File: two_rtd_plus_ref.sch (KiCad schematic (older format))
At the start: 18 parts

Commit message: completed schematic
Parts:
- C10, C11, C12, C13, C14, C15: renamed from C?; value C -> 5nF
- C7, C8, C9: renamed from C?; value C -> 50nF
- R10, R11, R12, R7, R8, R9: renamed from R?; value R -> 5k
- R6: renamed from R?; value R -> 2k
- gave numbers to parts that had none: 2

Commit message: finished schematic, assigned footprints, generated netlist
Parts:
- C10, C11, C12, C13, C14, C15, C7, C8, C9: footprint (none) -> Capacitor_SMD:C_0805_2012Metric_Pad1.15x1.40mm_HandSolder
- J3, J4: footprint (none) -> temp4x4:screw_term_4x
- R10, R11, R12, R6, R7, R8, R9: footprint (none) -> Resistor_SMD:R_0805_2012Metric_Pad1.15x1.40mm_HandSolder
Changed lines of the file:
@@
 AR Path="/5EC374D6/5EC48F50" Ref="J3"  Part="1"
 AR Path="/5ED0B429/5EC48F50" Ref="J5"  Part="1"
-F 0 "J5" H 3968 2917 50  0000 C CNN
+F 0 "J3" H 3968 2917 50  0000 C CNN
 F 1 "4-wire RTD" H 3968 2826 50  0000 C CNN
-F 2 "" H 4050 2600 50  0001 C CNN
+F 2 "temp4x4:screw_term_4x" H 4050 2600 50  0001 C CNN
 F 3 "~" H 4050 2600 50  0001 C CNN
 	1    4050 2600
@@
 AR Path="/5EC374D6/5EC48F56" Ref="C11"  Part="1"
 AR Path="/5ED0B429/5EC48F56" Ref="C20"  Part="1"
-F 0 "C20" H 5565 2846 50  0000 L CNN
+F 0 "C11" H 5565 2846 50  0000 L CNN
 F 1 "5nF" H 5565 2755 50  0000 L CNN
-F 2 "" H 5488 2650 50  0001 C CNN
+F 2 "Capacitor_SMD:C_0805_2012Metric_Pad1.15x1.40mm_HandSolder" H 5488 2650 50  0001 C CNN
 F 3 "~" H 5450 2800 50  0001 C CNN
 	1    5450 2800
@@
 AR Path="/5EC374D6/5EC48F5C" Ref="C7"  Part="1"
 AR Path="/5ED0B429/5EC48F5C" Ref="C16"  Part="1"
-F 0 "C16" H 5215 2696 50  0000 L CNN
+F 0 "C7" H 5215 2696 50  0000 L CNN
 F 1 "50nF" H 5215 2605 50  0000 L CNN
-F 2 "" H 5138 2500 50  0001 C CNN
+F 2 "Capacitor_SMD:C_0805_2012Metric_Pad1.15x1.40mm_HandSolder" H 5138 2500 50  0001 C CNN
 F 3 "~" H 5100 2650 50  0001 C CNN
 	1    5100 2650
@@
 AR Path="/5EC374D6/5EC48F62" Ref="C10"  Part="1"
 AR Path="/5ED0B429/5EC48F62" Ref="C19"  Part="1"
-F 0 "C19" H 5565 2546 50  0000 L CNN
+F 0 "C10" H 5565 2546 50  0000 L CNN
 F 1 "5nF" H 5565 2455 50  0000 L CNN
-F 2 "" H 5488 2350 50  0001 C CNN
+F 2 "Capacitor_SMD:C_0805_2012Metric_Pad1.15x1.40mm_HandSolder" H 5488 2350 50  0001 C CNN
 F 3 "~" H 5450 2500 50  0001 C CNN
 	1    5450 2500
@@
 AR Path="/5EC374D6/5EC48F68" Ref="#PWR014"  Part="1"
 AR Path="/5ED0B429/5EC48F68" Ref="#PWR017"  Part="1"
-F 0 "#PWR017" H 5650 2400 50  0001 C CNN
+F 0 "#PWR014" H 5650 2400 50  0001 C CNN
 F 1 "Earth" H 5650 2500 50  0001 C CNN
 F 2 "" H 5650 2650 50  0001 C CNN
@@
 AR Path="/5EC374D6/5EC48F74" Ref="R9"  Part="1"
 AR Path="/5ED0B429/5EC48F74" Ref="R16"  Part="1"
-F 0 "R16" V 5057 2350 50  0000 C CNN
+F 0 "R9" V 5057 2350 50  0000 C CNN
 F 1 "5k" V 4966 2350 50  0000 C CNN
-F 2 "" V 4780 2350 50  0001 C CNN
+F 2 "Resistor_SMD:R_0805_2012Metric_Pad1.15x1.40mm_HandSolder" V 4780 2350 50  0001 C CNN
 F 3 "~" H 4850 2350 50  0001 C CNN
 	1    4850 2350
@@
 AR Path="/5EC374D6/5EC48F7B" Ref="R10"  Part="1"
 AR Path="/5ED0B429/5EC48F7B" Ref="R17"  Part="1"
-F 0 "R17" V 5057 2950 50  0000 C CNN
+F 0 "R10" V 5057 2950 50  0000 C CNN
 F 1 "5k" V 4966 2950 50  0000 C CNN
-F 2 "" V 4780 2950 50  0001 C CNN
+F 2 "Resistor_SMD:R_0805_2012Metric_Pad1.15x1.40mm_HandSolder" V 4780 2950 50  0001 C CNN
 F 3 "~" H 4850 2950 50  0001 C CNN
 	1    4850 2950
@@
 AR Path="/5EC374D6/5EC48F91" Ref="J4"  Part="1"
 AR Path="/5ED0B429/5EC48F91" Ref="J6"  Part="1"
-F 0 "J6" H 3968 3967 50  0000 C CNN
+F 0 "J4" H 3968 3967 50  0000 C CNN
 F 1 "4-wire RTD" H 3968 3876 50  0000 C CNN
-F 2 "" H 4050 3650 50  0001 C CNN
+F 2 "temp4x4:screw_term_4x" H 4050 3650 50  0001 C CNN
 F 3 "~" H 4050 3650 50  0001 C CNN
 	1    4050 3650
@@
 AR Path="/5EC374D6/5EC48F97" Ref="C13"  Part="1"
 AR Path="/5ED0B429/5EC48F97" Ref="C22"  Part="1"
-F 0 "C22" H 5565 3896 50  0000 L CNN
+F 0 "C13" H 5565 3896 50  0000 L CNN
 F 1 "5nF" H 5565 3805 50  0000 L CNN
-F 2 "" H 5488 3700 50  0001 C CNN
+F 2 "Capacitor_SMD:C_0805_2012Metric_Pad1.15x1.40mm_HandSolder" H 5488 3700 50  0001 C CNN
 F 3 "~" H 5450 3850 50  0001 C CNN
 	1    5450 3850
@@
 AR Path="/5EC374D6/5EC48F9D" Ref="C8"  Part="1"
 AR Path="/5ED0B429/5EC48F9D" Ref="C17"  Part="1"
-F 0 "C17" H 5215 3746 50  0000 L CNN
+F 0 "C8" H 5215 3746 50  0000 L CNN
 F 1 "50nF" H 5215 3655 50  0000 L CNN
-F 2 "" H 5138 3550 50  0001 C CNN
+F 2 "Capacitor_SMD:C_0805_2012Metric_Pad1.15x1.40mm_HandSolder" H 5138 3550 50  0001 C CNN
 F 3 "~" H 5100 3700 50  0001 C CNN
 	1    5100 3700
@@
 AR Path="/5EC374D6/5EC48FA3" Ref="C12"  Part="1"
 AR Path="/5ED0B429/5EC48FA3" Ref="C21"  Part="1"
-F 0 "C21" H 5565 3596 50  0000 L CNN
+F 0 "C12" H 5565 3596 50  0000 L CNN
 F 1 "5nF" H 5565 3505 50  0000 L CNN
-F 2 "" H 5488 3400 50  0001 C CNN
+F 2 "Capacitor_SMD:C_0805_2012Metric_Pad1.15x1.40mm_HandSolder" H 5488 3400 50  0001 C CNN
 F 3 "~" H 5450 3550 50  0001 C CNN
 	1    5450 3550
@@
 AR Path="/5EC374D6/5EC48FA9" Ref="#PWR015"  Part="1"
 AR Path="/5ED0B429/5EC48FA9" Ref="#PWR018"  Part="1"
-F 0 "#PWR018" H 5650 3450 50  0001 C CNN
+F 0 "#PWR015" H 5650 3450 50  0001 C CNN
 F 1 "Earth" H 5650 3550 50  0001 C CNN
 F 2 "" H 5650 3700 50  0001 C CNN
@@
 AR Path="/5EC374D6/5EC48FB5" Ref="R11"  Part="1"
 AR Path="/5ED0B429/5EC48FB5" Ref="R18"  Part="1"
-F 0 "R18" V 5057 3400 50  0000 C CNN
+F 0 "R11" V 5057 3400 50  0000 C CNN
 F 1 "5k" V 4966 3400 50  0000 C CNN
-F 2 "" V 4780 3400 50  0001 C CNN
+F 2 "Resistor_SMD:R_0805_2012Metric_Pad1.15x1.40mm_HandSolder" V 4780 3400 50  0001 C CNN
 F 3 "~" H 4850 3400 50  0001 C CNN
 	1    4850 3400
@@
 AR Path="/5EC374D6/5EC48FBC" Ref="R12"  Part="1"
 AR Path="/5ED0B429/5EC48FBC" Ref="R19"  Part="1"
-F 0 "R19" V 5057 4000 50  0000 C CNN
+F 0 "R12" V 5057 4000 50  0000 C CNN
 F 1 "5k" V 4966 4000 50  0000 C CNN
-F 2 "" V 4780 4000 50  0001 C CNN
+F 2 "Resistor_SMD:R_0805_2012Metric_Pad1.15x1.40mm_HandSolder" V 4780 4000 50  0001 C CNN
 F 3 "~" H 4850 4000 50  0001 C CNN
 	1    4850 4000
@@
 AR Path="/5EC374D6/5EC48FD1" Ref="C15"  Part="1"
 AR Path="/5ED0B429/5EC48FD1" Ref="C24"  Part="1"
-F 0 "C24" H 5565 4946 50  0000 L CNN
+F 0 "C15" H 5565 4946 50  0000 L CNN
 F 1 "5nF" H 5565 4855 50  0000 L CNN
-F 2 "" H 5488 4750 50  0001 C CNN
+F 2 "Capacitor_SMD:C_0805_2012Metric_Pad1.15x1.40mm_HandSolder" H 5488 4750 50  0001 C CNN
 F 3 "~" H 5450 4900 50  0001 C CNN
 	1    5450 4900
@@
 AR Path="/5EC374D6/5EC48FD7" Ref="C9"  Part="1"
 AR Path="/5ED0B429/5EC48FD7" Ref="C18"  Part="1"
-F 0 "C18" H 5215 4796 50  0000 L CNN
+F 0 "C9" H 5215 4796 50  0000 L CNN
 F 1 "50nF" H 5215 4705 50  0000 L CNN
-F 2 "" H 5138 4600 50  0001 C CNN
+F 2 "Capacitor_SMD:C_0805_2012Metric_Pad1.15x1.40mm_HandSolder" H 5138 4600 50  0001 C CNN
 F 3 "~" H 5100 4750 50  0001 C CNN
 	1    5100 4750
@@
 AR Path="/5EC374D6/5EC48FDD" Ref="C14"  Part="1"
 AR Path="/5ED0B429/5EC48FDD" Ref="C23"  Part="1"
-F 0 "C23" H 5565 4646 50  0000 L CNN
+F 0 "C14" H 5565 4646 50  0000 L CNN
 F 1 "5nF" H 5565 4555 50  0000 L CNN
-F 2 "" H 5488 4450 50  0001 C CNN
+F 2 "Capacitor_SMD:C_0805_2012Metric_Pad1.15x1.40mm_HandSolder" H 5488 4450 50  0001 C CNN
 F 3 "~" H 5450 4600 50  0001 C CNN
 	1    5450 4600
@@
 AR Path="/5EC374D6/5EC48FE3" Ref="#PWR016"  Part="1"
 AR Path="/5ED0B429/5EC48FE3" Ref="#PWR019"  Part="1"
-F 0 "#PWR019" H 5650 4500 50  0001 C CNN
+F 0 "#PWR016" H 5650 4500 50  0001 C CNN
 F 1 "Earth" H 5650 4600 50  0001 C CNN
 F 2 "" H 5650 4750 50  0001 C CNN
@@
 AR Path="/5EC374D6/5EC48FEF" Ref="R7"  Part="1"
 AR Path="/5ED0B429/5EC48FEF" Ref="R14"  Part="1"
-F 0 "R14" V 5007 4450 50  0000 C CNN
+F 0 "R7" V 5007 4450 50  0000 C CNN
 F 1 "5k" V 4916 4450 50  0000 C CNN
-F 2 "" V 4730 4450 50  0001 C CNN
+F 2 "Resistor_SMD:R_0805_2012Metric_Pad1.15x1.40mm_HandSolder" V 4730 4450 50  0001 C CNN
 F 3 "~" H 4800 4450 50  0001 C CNN
 	1    4800 4450
@@
 AR Path="/5EC374D6/5EC48FF6" Ref="R8"  Part="1"
 AR Path="/5ED0B429/5EC48FF6" Ref="R15"  Part="1"
-F 0 "R15" V 5007 5050 50  0000 C CNN
+F 0 "R8" V 5007 5050 50  0000 C CNN
 F 1 "5k" V 4916 5050 50  0000 C CNN
-F 2 "" V 4730 5050 50  0001 C CNN
+F 2 "Resistor_SMD:R_0805_2012Metric_Pad1.15x1.40mm_HandSolder" V 4730 5050 50  0001 C CNN
 F 3 "~" H 4800 5050 50  0001 C CNN
 	1    4800 5050
@@
 AR Path="/5EC374D6/5EC49006" Ref="R6"  Part="1"
 AR Path="/5ED0B429/5EC49006" Ref="R13"  Part="1"
-F 0 "R13" H 4520 4796 50  0000 L CNN
+F 0 "R6" H 4520 4796 50  0000 L CNN
 F 1 "2k" H 4520 4705 50  0000 L CNN
-F 2 "" V 4380 4750 50  0001 C CNN
+F 2 "Resistor_SMD:R_0805_2012Metric_Pad1.15x1.40mm_HandSolder" V 4380 4750 50  0001 C CNN
 F 3 "~" H 4450 4750 50  0001 C CNN
 	1    4450 4750

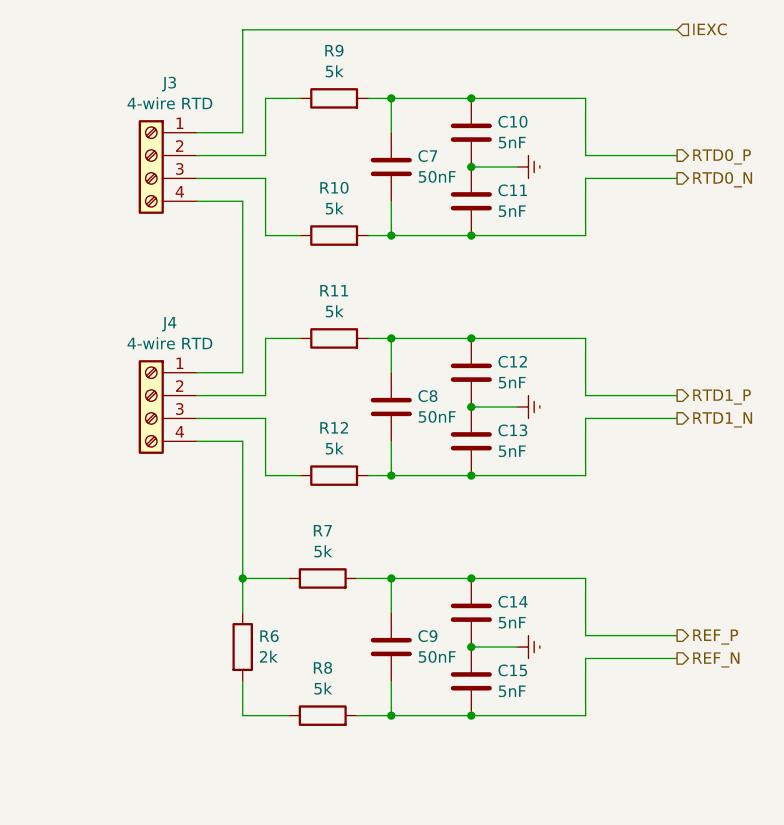
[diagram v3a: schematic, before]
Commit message: added jumper to bypass 2nd RTD
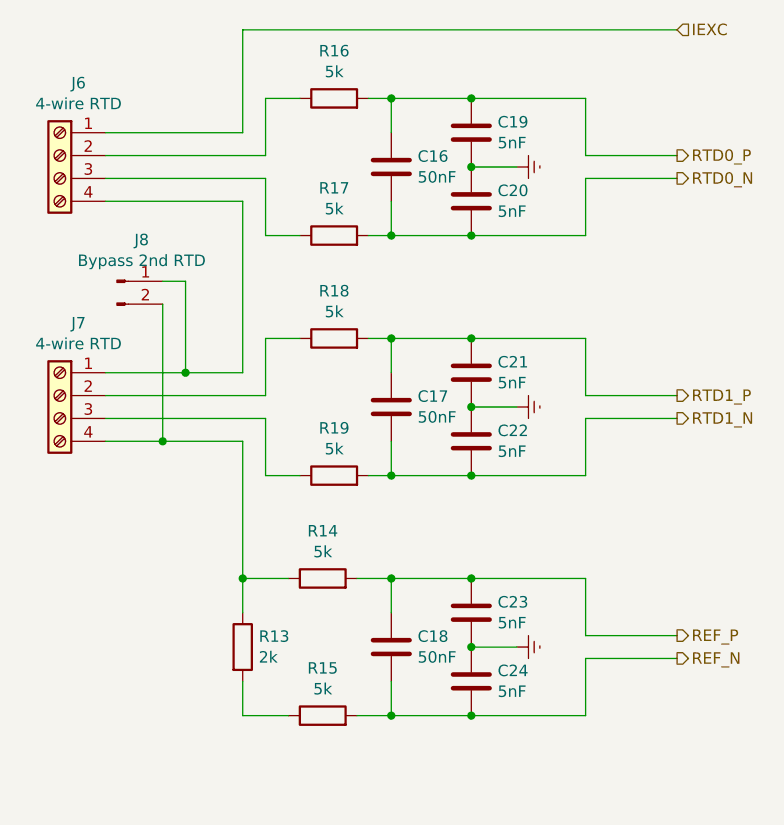
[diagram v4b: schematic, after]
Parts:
- added J5: Bypass 2nd RTD, symbol Connector:Conn_01x02_Male
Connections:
- net at J3.4 (Pin_4), J4.1 (Pin_1): now also J5.1 (Pin_1)
- net at J4.4 (Pin_4), R6.1, R7.1: now also J5.2 (Pin_2)
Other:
- moved on the sheet: J6, J7
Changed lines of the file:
@@
 L Connector:Screw_Terminal_01x04 J3
 U 1 1 5EC48F50
-P 4050 2600
+P 3650 2600
 AR Path="/5EC374D6/5EC48F50" Ref="J3"  Part="1"
-AR Path="/5ED0B429/5EC48F50" Ref="J5"  Part="1"
-F 0 "J3" H 3968 2917 50  0000 C CNN
-F 1 "4-wire RTD" H 3968 2826 50  0000 C CNN
-F 2 "temp4x4:screw_term_4x" H 4050 2600 50  0001 C CNN
-F 3 "~" H 4050 2600 50  0001 C CNN
-	1    4050 2600
+AR Path="/5ED0B429/5EC48F50" Ref="J6"  Part="1"
+F 0 "J6" H 3568 2917 50  0000 C CNN
+F 1 "4-wire RTD" H 3568 2826 50  0000 C CNN
+F 2 "temp4x4:screw_term_4x" H 3650 2600 50  0001 C CNN
+F 3 "~" H 3650 2600 50  0001 C CNN
+	1    3650 2600
 	-1   0    0    -1
 $EndComp
@@
 AR Path="/5EC374D6/5EC48F56" Ref="C11"  Part="1"
 AR Path="/5ED0B429/5EC48F56" Ref="C20"  Part="1"
-F 0 "C11" H 5565 2846 50  0000 L CNN
+F 0 "C20" H 5565 2846 50  0000 L CNN
 F 1 "5nF" H 5565 2755 50  0000 L CNN
 F 2 "Capacitor_SMD:C_0805_2012Metric_Pad1.15x1.40mm_HandSolder" H 5488 2650 50  0001 C CNN
@@
 AR Path="/5EC374D6/5EC48F5C" Ref="C7"  Part="1"
 AR Path="/5ED0B429/5EC48F5C" Ref="C16"  Part="1"
-F 0 "C7" H 5215 2696 50  0000 L CNN
+F 0 "C16" H 5215 2696 50  0000 L CNN
 F 1 "50nF" H 5215 2605 50  0000 L CNN
 F 2 "Capacitor_SMD:C_0805_2012Metric_Pad1.15x1.40mm_HandSolder" H 5138 2500 50  0001 C CNN
@@
 AR Path="/5EC374D6/5EC48F62" Ref="C10"  Part="1"
 AR Path="/5ED0B429/5EC48F62" Ref="C19"  Part="1"
-F 0 "C10" H 5565 2546 50  0000 L CNN
+F 0 "C19" H 5565 2546 50  0000 L CNN
 F 1 "5nF" H 5565 2455 50  0000 L CNN
 F 2 "Capacitor_SMD:C_0805_2012Metric_Pad1.15x1.40mm_HandSolder" H 5488 2350 50  0001 C CNN
@@
 AR Path="/5EC374D6/5EC48F68" Ref="#PWR014"  Part="1"
 AR Path="/5ED0B429/5EC48F68" Ref="#PWR017"  Part="1"
-F 0 "#PWR014" H 5650 2400 50  0001 C CNN
+F 0 "#PWR017" H 5650 2400 50  0001 C CNN
 F 1 "Earth" H 5650 2500 50  0001 C CNN
 F 2 "" H 5650 2650 50  0001 C CNN
@@
 AR Path="/5EC374D6/5EC48F74" Ref="R9"  Part="1"
 AR Path="/5ED0B429/5EC48F74" Ref="R16"  Part="1"
-F 0 "R9" V 5057 2350 50  0000 C CNN
+F 0 "R16" V 5057 2350 50  0000 C CNN
 F 1 "5k" V 4966 2350 50  0000 C CNN
 F 2 "Resistor_SMD:R_0805_2012Metric_Pad1.15x1.40mm_HandSolder" V 4780 2350 50  0001 C CNN
@@
 AR Path="/5EC374D6/5EC48F7B" Ref="R10"  Part="1"
 AR Path="/5ED0B429/5EC48F7B" Ref="R17"  Part="1"
-F 0 "R10" V 5057 2950 50  0000 C CNN
+F 0 "R17" V 5057 2950 50  0000 C CNN
 F 1 "5k" V 4966 2950 50  0000 C CNN
 F 2 "Resistor_SMD:R_0805_2012Metric_Pad1.15x1.40mm_HandSolder" V 4780 2950 50  0001 C CNN
@@
 Connection ~ 5100 2950
 Wire Wire Line
-	4250 2600 4550 2600
-Wire Wire Line
 	4550 2600 4550 2350
 Wire Wire Line
 	4550 2350 4700 2350
-Wire Wire Line
-	4250 2700 4550 2700
 Wire Wire Line
 	4550 2700 4550 2950
@@
 L Connector:Screw_Terminal_01x04 J4
 U 1 1 5EC48F91
-P 4050 3650
+P 3650 3650
 AR Path="/5EC374D6/5EC48F91" Ref="J4"  Part="1"
-AR Path="/5ED0B429/5EC48F91" Ref="J6"  Part="1"
-F 0 "J4" H 3968 3967 50  0000 C CNN
-F 1 "4-wire RTD" H 3968 3876 50  0000 C CNN
-F 2 "temp4x4:screw_term_4x" H 4050 3650 50  0001 C CNN
-F 3 "~" H 4050 3650 50  0001 C CNN
-	1    4050 3650
+AR Path="/5ED0B429/5EC48F91" Ref="J7"  Part="1"
+F 0 "J7" H 3568 3967 50  0000 C CNN
+F 1 "4-wire RTD" H 3568 3876 50  0000 C CNN
+F 2 "temp4x4:screw_term_4x" H 3650 3650 50  0001 C CNN
+F 3 "~" H 3650 3650 50  0001 C CNN
+	1    3650 3650
 	-1   0    0    -1
 $EndComp
@@
 AR Path="/5EC374D6/5EC48F97" Ref="C13"  Part="1"
 AR Path="/5ED0B429/5EC48F97" Ref="C22"  Part="1"
-F 0 "C13" H 5565 3896 50  0000 L CNN
+F 0 "C22" H 5565 3896 50  0000 L CNN
 F 1 "5nF" H 5565 3805 50  0000 L CNN
 F 2 "Capacitor_SMD:C_0805_2012Metric_Pad1.15x1.40mm_HandSolder" H 5488 3700 50  0001 C CNN
@@
 AR Path="/5EC374D6/5EC48F9D" Ref="C8"  Part="1"
 AR Path="/5ED0B429/5EC48F9D" Ref="C17"  Part="1"
-F 0 "C8" H 5215 3746 50  0000 L CNN
+F 0 "C17" H 5215 3746 50  0000 L CNN
 F 1 "50nF" H 5215 3655 50  0000 L CNN
 F 2 "Capacitor_SMD:C_0805_2012Metric_Pad1.15x1.40mm_HandSolder" H 5138 3550 50  0001 C CNN
@@
 AR Path="/5EC374D6/5EC48FA3" Ref="C12"  Part="1"
 AR Path="/5ED0B429/5EC48FA3" Ref="C21"  Part="1"
-F 0 "C12" H 5565 3596 50  0000 L CNN
+F 0 "C21" H 5565 3596 50  0000 L CNN
 F 1 "5nF" H 5565 3505 50  0000 L CNN
 F 2 "Capacitor_SMD:C_0805_2012Metric_Pad1.15x1.40mm_HandSolder" H 5488 3400 50  0001 C CNN
@@
 AR Path="/5EC374D6/5EC48FA9" Ref="#PWR015"  Part="1"
 AR Path="/5ED0B429/5EC48FA9" Ref="#PWR018"  Part="1"
-F 0 "#PWR015" H 5650 3450 50  0001 C CNN
+F 0 "#PWR018" H 5650 3450 50  0001 C CNN
 F 1 "Earth" H 5650 3550 50  0001 C CNN
 F 2 "" H 5650 3700 50  0001 C CNN
@@
 AR Path="/5EC374D6/5EC48FB5" Ref="R11"  Part="1"
 AR Path="/5ED0B429/5EC48FB5" Ref="R18"  Part="1"
-F 0 "R11" V 5057 3400 50  0000 C CNN
+F 0 "R18" V 5057 3400 50  0000 C CNN
 F 1 "5k" V 4966 3400 50  0000 C CNN
 F 2 "Resistor_SMD:R_0805_2012Metric_Pad1.15x1.40mm_HandSolder" V 4780 3400 50  0001 C CNN
@@
 AR Path="/5EC374D6/5EC48FBC" Ref="R12"  Part="1"
 AR Path="/5ED0B429/5EC48FBC" Ref="R19"  Part="1"
-F 0 "R12" V 5057 4000 50  0000 C CNN
+F 0 "R19" V 5057 4000 50  0000 C CNN
 F 1 "5k" V 4966 4000 50  0000 C CNN
 F 2 "Resistor_SMD:R_0805_2012Metric_Pad1.15x1.40mm_HandSolder" V 4780 4000 50  0001 C CNN
@@
 Connection ~ 5100 4000
 Wire Wire Line
-	4250 3650 4550 3650
-Wire Wire Line
 	4550 3650 4550 3400
 Wire Wire Line
 	4550 3400 4700 3400
-Wire Wire Line
-	4250 3750 4550 3750
 Wire Wire Line
 	4550 3750 4550 4000
@@
 AR Path="/5EC374D6/5EC48FD1" Ref="C15"  Part="1"
 AR Path="/5ED0B429/5EC48FD1" Ref="C24"  Part="1"
-F 0 "C15" H 5565 4946 50  0000 L CNN
+F 0 "C24" H 5565 4946 50  0000 L CNN
 F 1 "5nF" H 5565 4855 50  0000 L CNN
 F 2 "Capacitor_SMD:C_0805_2012Metric_Pad1.15x1.40mm_HandSolder" H 5488 4750 50  0001 C CNN
@@
 AR Path="/5EC374D6/5EC48FD7" Ref="C9"  Part="1"
 AR Path="/5ED0B429/5EC48FD7" Ref="C18"  Part="1"
-F 0 "C9" H 5215 4796 50  0000 L CNN
+F 0 "C18" H 5215 4796 50  0000 L CNN
 F 1 "50nF" H 5215 4705 50  0000 L CNN
 F 2 "Capacitor_SMD:C_0805_2012Metric_Pad1.15x1.40mm_HandSolder" H 5138 4600 50  0001 C CNN
@@
 AR Path="/5EC374D6/5EC48FDD" Ref="C14"  Part="1"
 AR Path="/5ED0B429/5EC48FDD" Ref="C23"  Part="1"
-F 0 "C14" H 5565 4646 50  0000 L CNN
+F 0 "C23" H 5565 4646 50  0000 L CNN
 F 1 "5nF" H 5565 4555 50  0000 L CNN
 F 2 "Capacitor_SMD:C_0805_2012Metric_Pad1.15x1.40mm_HandSolder" H 5488 4450 50  0001 C CNN
@@
 AR Path="/5EC374D6/5EC48FE3" Ref="#PWR016"  Part="1"
 AR Path="/5ED0B429/5EC48FE3" Ref="#PWR019"  Part="1"
-F 0 "#PWR016" H 5650 4500 50  0001 C CNN
+F 0 "#PWR019" H 5650 4500 50  0001 C CNN
 F 1 "Earth" H 5650 4600 50  0001 C CNN
 F 2 "" H 5650 4750 50  0001 C CNN
@@
 AR Path="/5EC374D6/5EC48FEF" Ref="R7"  Part="1"
 AR Path="/5ED0B429/5EC48FEF" Ref="R14"  Part="1"
-F 0 "R7" V 5007 4450 50  0000 C CNN
+F 0 "R14" V 5007 4450 50  0000 C CNN
 F 1 "5k" V 4916 4450 50  0000 C CNN
 F 2 "Resistor_SMD:R_0805_2012Metric_Pad1.15x1.40mm_HandSolder" V 4730 4450 50  0001 C CNN
@@
 AR Path="/5EC374D6/5EC48FF6" Ref="R8"  Part="1"
 AR Path="/5ED0B429/5EC48FF6" Ref="R15"  Part="1"
-F 0 "R8" V 5007 5050 50  0000 C CNN
+F 0 "R15" V 5007 5050 50  0000 C CNN
 F 1 "5k" V 4916 5050 50  0000 C CNN
 F 2 "Resistor_SMD:R_0805_2012Metric_Pad1.15x1.40mm_HandSolder" V 4730 5050 50  0001 C CNN
@@
 AR Path="/5EC374D6/5EC49006" Ref="R6"  Part="1"
 AR Path="/5ED0B429/5EC49006" Ref="R13"  Part="1"
-F 0 "R6" H 4520 4796 50  0000 L CNN
+F 0 "R13" H 4520 4796 50  0000 L CNN
 F 1 "2k" H 4520 4705 50  0000 L CNN
 F 2 "Resistor_SMD:R_0805_2012Metric_Pad1.15x1.40mm_HandSolder" V 4380 4750 50  0001 C CNN
@@
 	4450 2050 4450 2500
 Wire Wire Line
-	4450 2500 4250 2500
-Wire Wire Line
-	4250 2800 4450 2800
-Wire Wire Line
 	4450 2800 4450 3550
-Wire Wire Line
-	4450 3550 4250 3550
-Wire Wire Line
-	4250 3850 4450 3850
 Wire Wire Line
 	4450 3850 4450 4450
@@
 Text HLabel 6350 4800 2    50   Output ~ 0
 REF_N
+Wire Wire Line
+	3850 2500 4450 2500
+Wire Wire Line
+	3850 2600 4550 2600
+Wire Wire Line
+	3850 2700 4550 2700
+Wire Wire Line
+	3850 2800 4450 2800
+Wire Wire Line
+	3850 3550 4200 3550
+Wire Wire Line
+	3850 3650 4550 3650
+Wire Wire Line
+	3850 3750 4550 3750
+Wire Wire Line
+	3850 3850 4100 3850
+$Comp
+L Connector:Conn_01x02_Male J5
+U 1 1 5ECF80D6
+P 3900 3150
+AR Path="/5EC374D6/5ECF80D6" Ref="J5"  Part="1"
+AR Path="/5ED0B429/5ECF80D6" Ref="J8"  Part="1"
+F 0 "J8" H 4008 3331 50  0000 C CNN
+F 1 "Bypass 2nd RTD" H 4008 3240 50  0000 C CNN
+F 2 "" H 3900 3150 50  0001 C CNN
+F 3 "~" H 3900 3150 50  0001 C CNN
+	1    3900 3150
+	1    0    0    -1
+$EndComp
+Wire Wire Line
+	4100 3150 4200 3150
+Wire Wire Line
+	4200 3150 4200 3550
+Connection ~ 4200 3550
+Wire Wire Line
+	4200 3550 4450 3550
+Wire Wire Line
+	4100 3250 4100 3850
+Connection ~ 4100 3850
+Wire Wire Line
+	4100 3850 4450 3850
 $EndSCHEMATC
